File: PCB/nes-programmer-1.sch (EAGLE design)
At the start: 32 parts, among them J3 Molex 22-28-8062, M1 ATmega328P Module, M2 0124A, SW1 Push Switch, U1 MCP23S08, U2 MCP23S17

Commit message: Final tweaks.
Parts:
- added ACT: (no value), led:SMT0603
- added R18: 2K, rlc:RESISTOR0603
- renumbered J3 to SERIAL, SW1 to RESET
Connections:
- new net ACTIVITY: M1.D6, R18.1
- new net ACT_LED: ACT.A, R18.2
- net GND: now also ACT.C
- net SD_!DET: now also M1.D7; no longer M1.D6
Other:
- note added: "Mnemosyne"
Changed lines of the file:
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@@
 <part name="FRAME1" library="frames-custom" library_urn="urn:adsk.eagle:library:11820551" deviceset="LETTER_L" device="">
 <attribute name="DOCUMENT_NUMBER" value="NES-Programmer-1"/>
+<attribute name="REV" value="A"/>
 </part>
 <part name="CART" library="game-cartridge" library_urn="urn:adsk.eagle:library:42577318" deviceset="NES-RECEPTACLE" device="-VT-THD" value="NES Cart Slot, 72P, VT, THD"/>
@@
 <part name="R11" library="rlc" library_urn="urn:adsk.eagle:library:4192893" deviceset="RESISTOR" device="0603" package3d_urn="urn:adsk.eagle:package:4193040/5" value="10K"/>
 <part name="SUPPLY29" library="supply" library_urn="urn:adsk.eagle:library:10485988" deviceset="VCC" device=""/>
-<part name="SW1" library="switch-smd" library_urn="urn:adsk.eagle:library:5542824" deviceset="PUSHBTN-MOM" device="B3SN" package3d_urn="urn:adsk.eagle:package:5542863/3" value="Push Switch"/>
+<part name="RESET" library="switch-smd" library_urn="urn:adsk.eagle:library:5542824" deviceset="PUSHBTN-MOM" device="B3SN" package3d_urn="urn:adsk.eagle:package:5542863/3" value="Push Switch"/>
 <part name="SUPPLY30" library="supply" library_urn="urn:adsk.eagle:library:10485988" deviceset="GND" device=""/>
 <part name="SUPPLY31" library="supply" library_urn="urn:adsk.eagle:library:10485988" deviceset="VCC" device=""/>
@@
 <part name="R14" library="rlc" library_urn="urn:adsk.eagle:library:4192893" deviceset="RESISTOR" device="0603" package3d_urn="urn:adsk.eagle:package:4193040/5" value="4.7K"/>
 <part name="R15" library="rlc" library_urn="urn:adsk.eagle:library:4192893" deviceset="RESISTOR" device="0603" package3d_urn="urn:adsk.eagle:package:4193040/5" value="4.7K"/>
-<part name="J3" library="con-headers" library_urn="urn:adsk.eagle:library:5539071" deviceset="CON_06X1" device="-RA" package3d_urn="urn:adsk.eagle:package:5535171/6" value="Molex 22-28-8062"/>
+<part name="SERIAL" library="con-headers" library_urn="urn:adsk.eagle:library:5539071" deviceset="CON_06X1" device="-RA" package3d_urn="urn:adsk.eagle:package:5535171/6" value="Molex 22-28-8062"/>
 <part name="SUPPLY34" library="supply" library_urn="urn:adsk.eagle:library:10485988" deviceset="GND" device=""/>
 <part name="SUPPLY35" library="supply" library_urn="urn:adsk.eagle:library:10485988" deviceset="VCC" device=""/>
@@
 <part name="SUPPLY40" library="supply" library_urn="urn:adsk.eagle:library:10485988" deviceset="GND" device=""/>
 <part name="VR33" library="regulators" library_urn="urn:adsk.eagle:library:7189770" deviceset="LDO-3P-" device="-3.3V-SOT23" package3d_urn="urn:adsk.eagle:package:7189794/5" value="3.3V"/>
+<part name="ACT" library="led" library_urn="urn:adsk.eagle:library:5499911" deviceset="SMT" device="0603" package3d_urn="urn:adsk.eagle:package:5499947/3"/>
+<part name="R18" library="rlc" library_urn="urn:adsk.eagle:library:4192893" deviceset="RESISTOR" device="0603" package3d_urn="urn:adsk.eagle:package:4193040/5" value="2K"/>
+<part name="SUPPLY41" library="supply" library_urn="urn:adsk.eagle:library:10485988" deviceset="GND" device=""/>
 </parts>
 <sheets>
@@
 <text x="106.68" y="147.32" size="1.016" layer="97" align="center-right">SDA</text>
 <text x="106.68" y="149.86" size="1.016" layer="97" align="center-right">SCL</text>
+<text x="83.82" y="7.62" size="5.08" layer="97">Mnemosyne</text>
 </plain>
 <instances>
-<instance part="FRAME1" gate="G$1" x="0" y="0" smashed="yes"/>
+<instance part="FRAME1" gate="G$1" x="0" y="0" smashed="yes">
+<attribute name="REV" x="240.538" y="7.112" size="3.81" layer="96"/>
+</instance>
 <instance part="FRAME1" gate="G$2" x="147.32" y="0" smashed="yes">
 <attribute name="LAST_DATE_TIME" x="160.02" y="1.27" size="2.54" layer="94" font="vector"/>
@@
 <attribute name="DRAWING_NAME" x="91.44" y="1.27" size="2.54" layer="94" font="vector" ratio="15"/>
 <attribute name="DOCUMENT_NUMBER" x="160.02" y="6.096" size="3.81" layer="94" ratio="15"/>
+<attribute name="REV" x="147.32" y="0" size="1.778" layer="96" display="off"/>
 </instance>
 <instance part="CART" gate="G$1" x="200.66" y="68.58" smashed="yes">
@@
 <attribute name="VALUE" x="101.6" y="176.657" size="1.27" layer="96" font="vector" ratio="15" align="bottom-center"/>
 </instance>
-<instance part="SW1" gate="G$1" x="96.52" y="160.02" smashed="yes" rot="R90">
+<instance part="RESET" gate="G$1" x="96.52" y="160.02" smashed="yes" rot="R90">
 <attribute name="NAME" x="93.726" y="160.02" size="1.27" layer="95" ratio="15" rot="R90" align="bottom-center"/>
 <attribute name="VALUE" x="97.536" y="160.02" size="0.6096" layer="96" rot="R90" align="top-center"/>
@@
 <attribute name="VALUE" x="99.06" y="146.05" size="0.9652" layer="96" font="vector" rot="R90" align="center"/>
 </instance>
-<instance part="J3" gate="1" x="12.7" y="134.62" smashed="yes">
+<instance part="SERIAL" gate="1" x="12.7" y="134.62" smashed="yes">
 <attribute name="VALUE" x="11.43" y="133.096" size="1.016" layer="96" rot="R90" align="center"/>
 <attribute name="NAME" x="12.192" y="142.24" size="1.778" layer="95" ratio="15" align="center"/>
@@
 <attribute name="VALUE" x="33.02" y="16.51" size="1.27" layer="96" align="bottom-center"/>
 <attribute name="NAME" x="33.02" y="19.812" size="1.778" layer="95" font="vector" ratio="15" align="center"/>
+</instance>
+<instance part="ACT" gate="G$1" x="167.64" y="152.4" smashed="yes">
+<attribute name="NAME" x="167.386" y="150.622" size="1.143" layer="95" font="vector" ratio="15" align="center"/>
+<attribute name="VALUE" x="167.132" y="154.051" size="0.8128" layer="96" font="vector" rot="MR0" align="center-left"/>
+</instance>
+<instance part="R18" gate="G$1" x="154.94" y="152.4" smashed="yes">
+<attribute name="NAME" x="156.21" y="153.6192" size="1.27" layer="95" font="vector" ratio="15" align="bottom-center"/>
+<attribute name="VALUE" x="156.21" y="152.4" size="0.9652" layer="96" font="vector" align="center"/>
+</instance>
+<instance part="SUPPLY41" gate="GND" x="170.18" y="149.86" smashed="yes">
+<attribute name="VALUE" x="170.18" y="147.193" size="0.6096" layer="96" font="vector" align="center"/>
 </instance>
 </instances>
@@
 </segment>
 <segment>
-<pinref part="SW1" gate="G$1" pin="1"/>
+<pinref part="RESET" gate="G$1" pin="1"/>
 <pinref part="SUPPLY30" gate="GND" pin="GND"/>
 <wire x1="96.52" y1="157.48" x2="96.52" y2="154.94" width="0.1524" layer="91"/>
@@
 </segment>
 <segment>
-<pinref part="J3" gate="1" pin="1"/>
+<pinref part="SERIAL" gate="1" pin="1"/>
 <pinref part="SUPPLY34" gate="GND" pin="GND"/>
 <wire x1="20.32" y1="139.7" x2="30.48" y2="139.7" width="0.1524" layer="91"/>
@@
 <pinref part="SUPPLY40" gate="GND" pin="GND"/>
 <wire x1="48.26" y1="7.62" x2="48.26" y2="5.08" width="0.1524" layer="91"/>
+</segment>
+<segment>
+<pinref part="SUPPLY41" gate="GND" pin="GND"/>
+<pinref part="ACT" gate="G$1" pin="C"/>
+<wire x1="170.18" y1="149.86" x2="170.18" y2="152.4" width="0.1524" layer="91"/>
 </segment>
 </net>
@@
 </segment>
 <segment>
-<pinref part="J3" gate="1" pin="3"/>
+<pinref part="SERIAL" gate="1" pin="3"/>
 <wire x1="20.32" y1="134.62" x2="22.86" y2="134.62" width="0.1524" layer="91"/>
 <pinref part="SUPPLY35" gate="G$1" pin="VCC"/>
@@
 <junction x="101.6" y="165.1"/>
 <label x="93.98" y="165.1" size="1.27" layer="95" rot="R180" xref="yes"/>
-<pinref part="SW1" gate="G$1" pin="2"/>
+<pinref part="RESET" gate="G$1" pin="2"/>
 <wire x1="96.52" y1="162.56" x2="96.52" y2="165.1" width="0.1524" layer="91"/>
 <wire x1="101.6" y1="165.1" x2="96.52" y2="165.1" width="0.1524" layer="91"/>
@@
 </segment>
 <segment>
-<label x="134.62" y="152.4" size="1.27" layer="95" xref="yes"/>
-<pinref part="M1" gate="G$1" pin="D6"/>
-<wire x1="129.54" y1="152.4" x2="134.62" y2="152.4" width="0.1524" layer="91"/>
+<label x="134.62" y="154.94" size="1.27" layer="95" xref="yes"/>
+<pinref part="M1" gate="G$1" pin="D7"/>
+<wire x1="129.54" y1="154.94" x2="134.62" y2="154.94" width="0.1524" layer="91"/>
 </segment>
 </net>
 <net name="FT_TX" class="0">
 <segment>
-<pinref part="J3" gate="1" pin="4"/>
+<pinref part="SERIAL" gate="1" pin="4"/>
 <wire x1="20.32" y1="132.08" x2="27.94" y2="132.08" width="0.1524" layer="91"/>
 <label x="20.066" y="132.588" size="1.27" layer="95"/>
@@
 <net name="FT_RX" class="0">
 <segment>
-<pinref part="J3" gate="1" pin="5"/>
+<pinref part="SERIAL" gate="1" pin="5"/>
 <wire x1="20.32" y1="129.54" x2="27.94" y2="129.54" width="0.1524" layer="91"/>
 <label x="20.066" y="129.794" size="1.27" layer="95"/>
@@
 </segment>
 </net>
+<net name="ACTIVITY" class="0">
+<segment>
+<pinref part="M1" gate="G$1" pin="D6"/>
+<wire x1="129.54" y1="152.4" x2="152.4" y2="152.4" width="0.1524" layer="91"/>
+<pinref part="R18" gate="G$1" pin="1"/>
+<label x="144.78" y="152.654" size="1.27" layer="95"/>
+</segment>
+</net>
+<net name="ACT_LED" class="0">
+<segment>
+<pinref part="R18" gate="G$1" pin="2"/>
+<pinref part="ACT" gate="G$1" pin="A"/>
+<wire x1="160.02" y1="152.4" x2="165.1" y2="152.4" width="0.1524" layer="91"/>
+<label x="160.02" y="152.654" size="0.762" layer="95"/>
+</segment>
+</net>

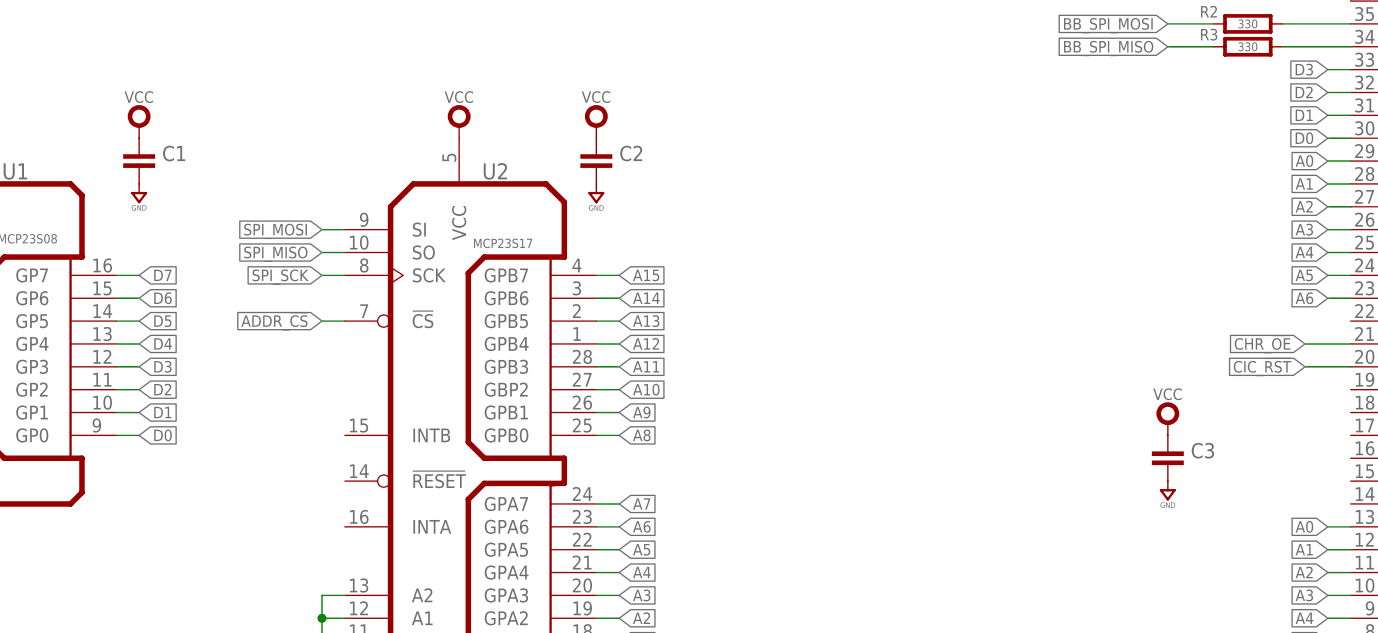
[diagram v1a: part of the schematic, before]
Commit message: Added Cap values, bump rev due to PCB change.
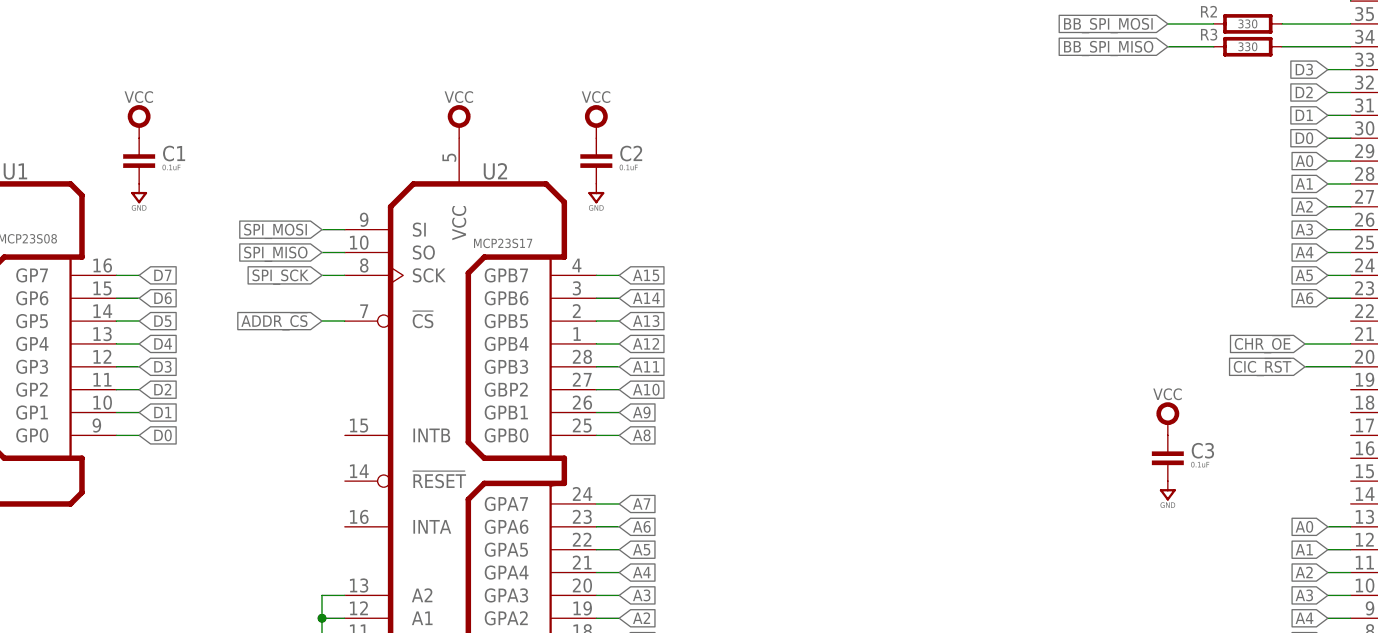
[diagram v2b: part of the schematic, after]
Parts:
- C1, C2, C3: value (none) -> 0.1uF
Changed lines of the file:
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@@
 <part name="FRAME1" library="frames-custom" library_urn="urn:adsk.eagle:library:11820551" deviceset="LETTER_L" device="">
 <attribute name="DOCUMENT_NUMBER" value="NES-Programmer-1"/>
-<attribute name="REV" value="A"/>
+<attribute name="REV" value="B"/>
 </part>
 <part name="CART" library="game-cartridge" library_urn="urn:adsk.eagle:library:42577318" deviceset="NES-RECEPTACLE" device="-VT-THD" value="NES Cart Slot, 72P, VT, THD"/>
 <part name="SUPPLY2" library="supply" library_urn="urn:adsk.eagle:library:10485988" deviceset="GND" device=""/>
 <part name="SUPPLY3" library="supply" library_urn="urn:adsk.eagle:library:10485988" deviceset="VCC" device=""/>
-<part name="C1" library="rlc" library_urn="urn:adsk.eagle:library:4192893" deviceset="CAPACITOR" device="0603" package3d_urn="urn:adsk.eagle:package:4193021/5"/>
+<part name="C1" library="rlc" library_urn="urn:adsk.eagle:library:4192893" deviceset="CAPACITOR" device="0603" package3d_urn="urn:adsk.eagle:package:4193021/5" value="0.1uF"/>
 <part name="SUPPLY5" library="supply" library_urn="urn:adsk.eagle:library:10485988" deviceset="VCC" device=""/>
 <part name="SUPPLY6" library="supply" library_urn="urn:adsk.eagle:library:10485988" deviceset="GND" device=""/>
-<part name="C2" library="rlc" library_urn="urn:adsk.eagle:library:4192893" deviceset="CAPACITOR" device="0603" package3d_urn="urn:adsk.eagle:package:4193021/5"/>
+<part name="C2" library="rlc" library_urn="urn:adsk.eagle:library:4192893" deviceset="CAPACITOR" device="0603" package3d_urn="urn:adsk.eagle:package:4193021/5" value="0.1uF"/>
 <part name="SUPPLY9" library="supply" library_urn="urn:adsk.eagle:library:10485988" deviceset="VCC" device=""/>
 <part name="SUPPLY10" library="supply" library_urn="urn:adsk.eagle:library:10485988" deviceset="GND" device=""/>
-<part name="C3" library="rlc" library_urn="urn:adsk.eagle:library:4192893" deviceset="CAPACITOR" device="0603" package3d_urn="urn:adsk.eagle:package:4193021/5"/>
+<part name="C3" library="rlc" library_urn="urn:adsk.eagle:library:4192893" deviceset="CAPACITOR" device="0603" package3d_urn="urn:adsk.eagle:package:4193021/5" value="0.1uF"/>
 <part name="SUPPLY13" library="supply" library_urn="urn:adsk.eagle:library:10485988" deviceset="VCC" device=""/>
 <part name="SUPPLY14" library="supply" library_urn="urn:adsk.eagle:library:10485988" deviceset="GND" device=""/>
